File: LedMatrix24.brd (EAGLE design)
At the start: 160 x 100 mm, 87 parts, among them IC1 74HC595N, IC11 74HC595N, IC2 74HC595N, IC3 74HC595N, IC4 UDN2981A, IC5 UDN2981A, IC6 74HC595N, IC8 UDN2981A, IC9 74HC595N

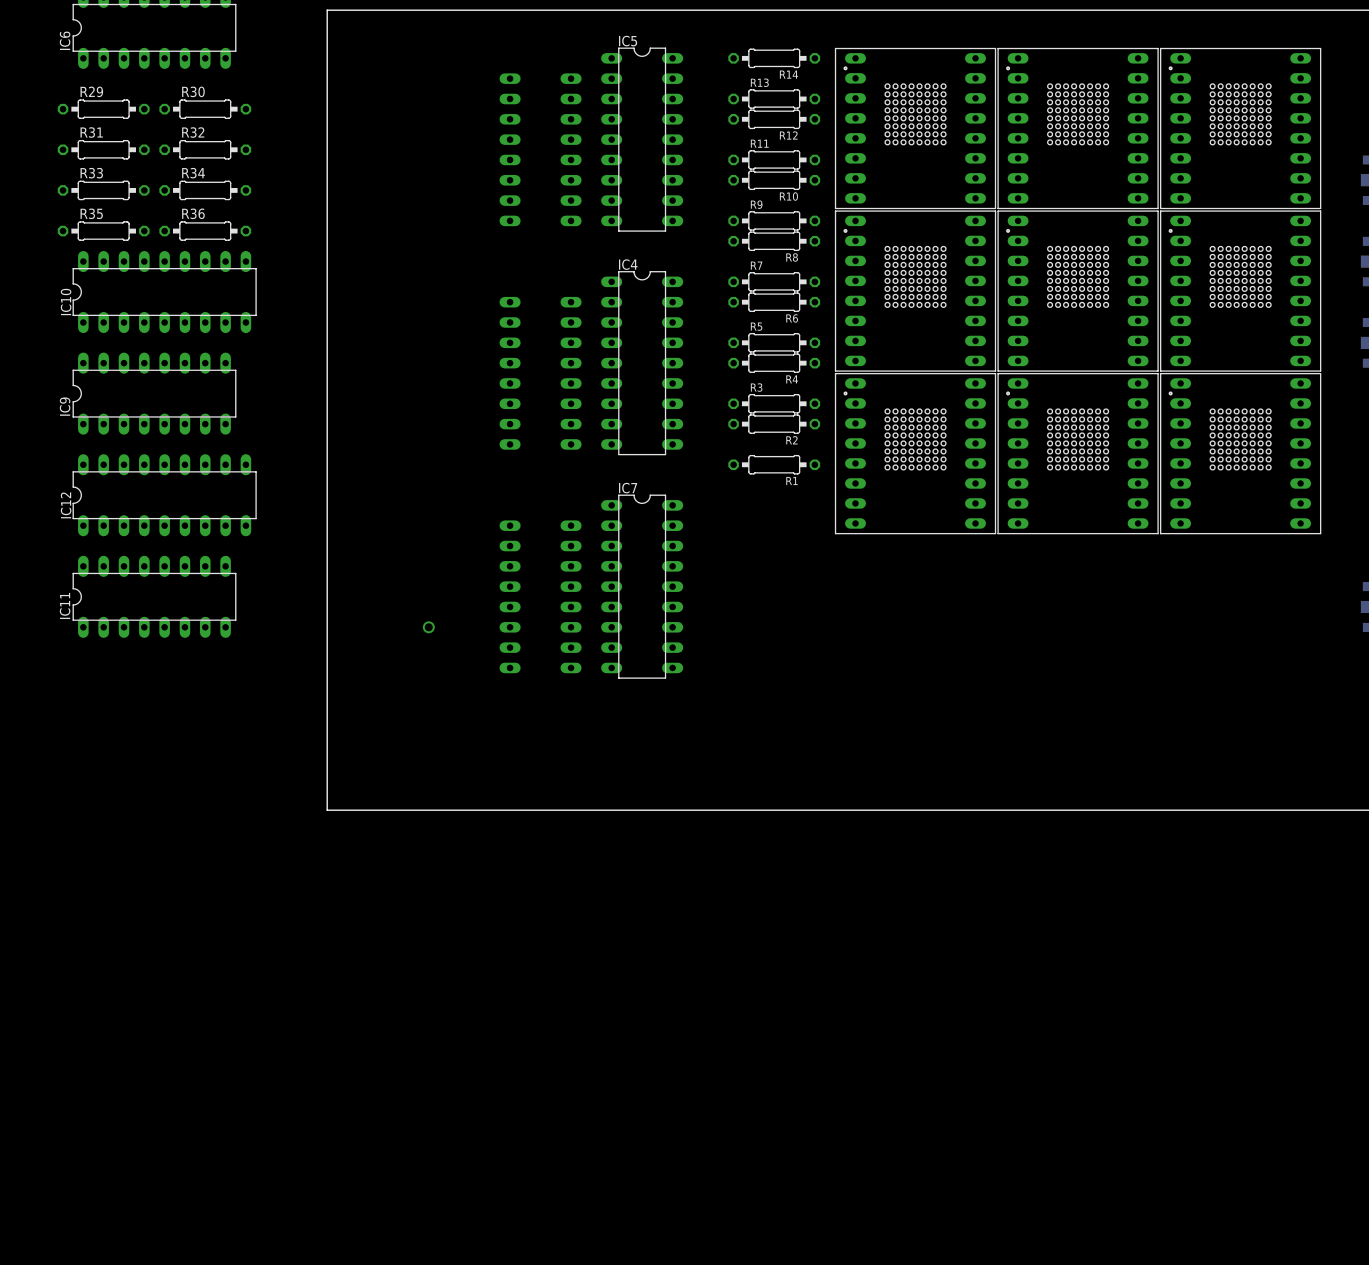
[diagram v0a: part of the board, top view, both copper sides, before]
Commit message: LED Matrizen an Raster 2.5mm angepasst und Buzzer eingefügt
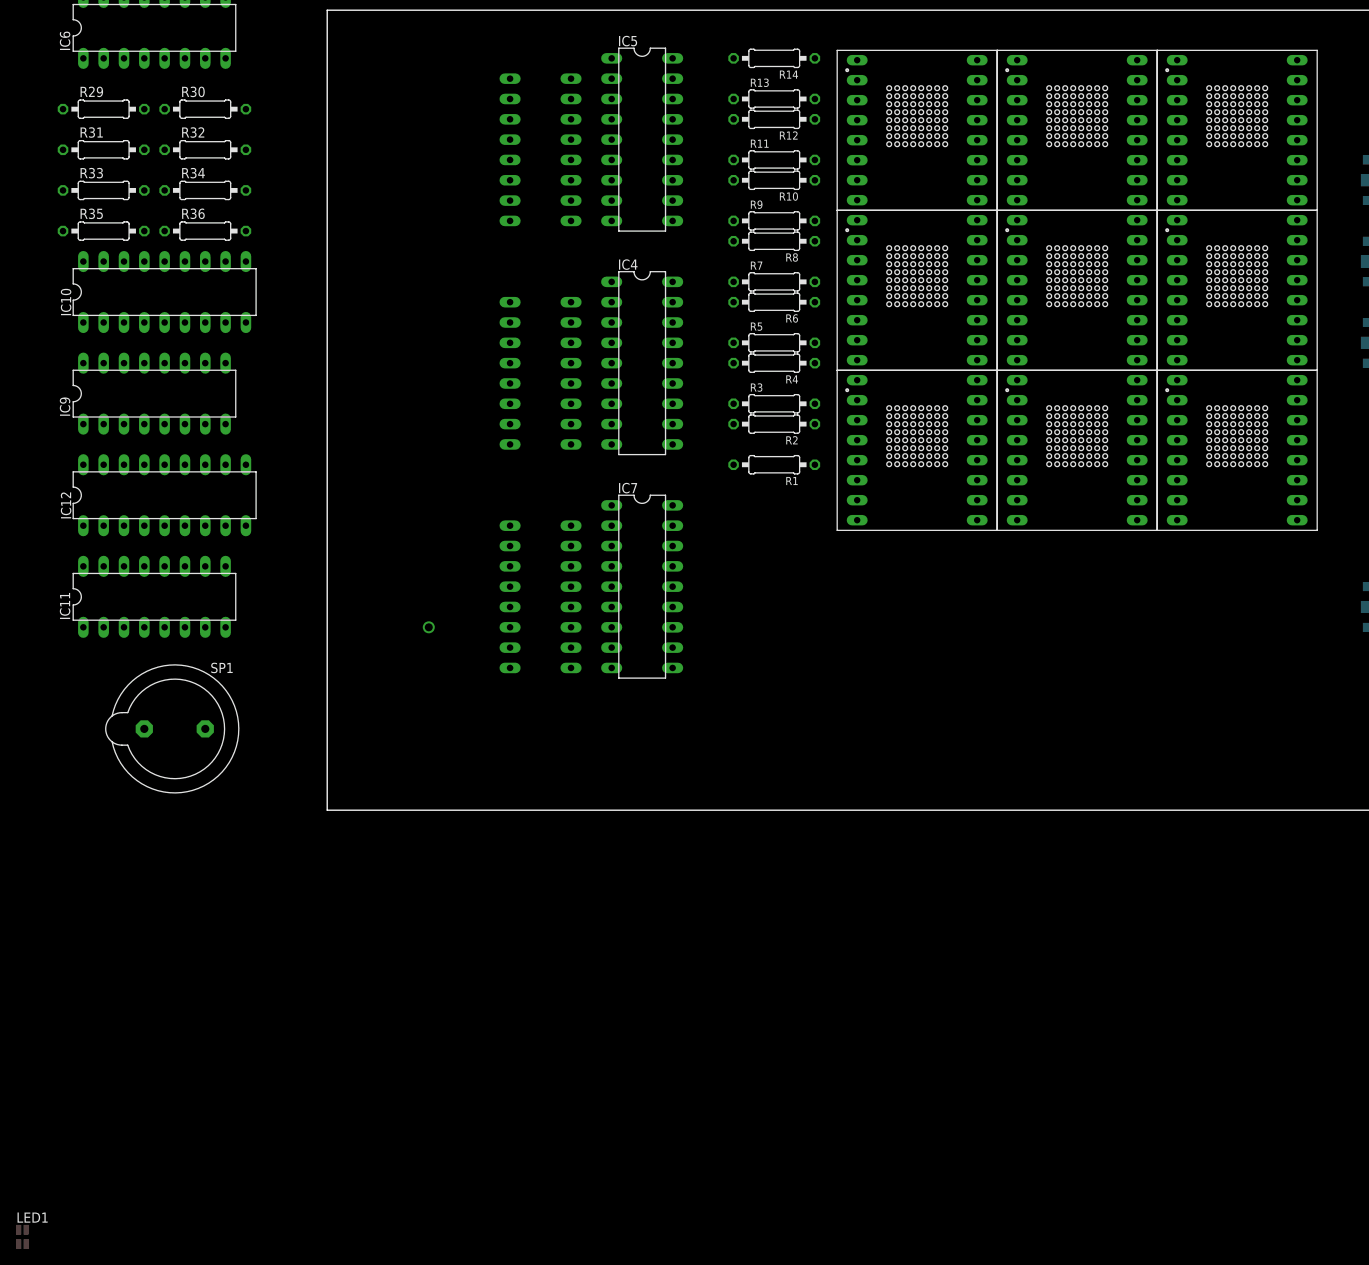
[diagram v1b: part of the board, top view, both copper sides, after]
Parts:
- added LED1: GM1WA55311A, led:GM1WA55311A
- added SP1: F/HGP, buzzer:F/HGP
- moved U$9 0.59 mm to (106.2, 53.8)
- moved U$3 0.49 mm to (106.2, 93.8)
- moved U$7 0.46 mm to (66.2, 53.8)
- moved U$6 0.44 mm to (106.2, 73.8)
- moved U$8 0.42 mm to (86.2, 53.8)
- moved U$1 0.31 mm to (66.2, 93.8)
- moved U$2 0.25 mm to (86.2, 93.8)
- moved U$4 0.23 mm to (66.2, 73.8)
- moved U$5 0.14 mm to (86.2, 73.8)
